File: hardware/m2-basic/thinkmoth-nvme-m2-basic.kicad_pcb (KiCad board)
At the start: 4 copper layers, 31 x 68.4 mm, 24 parts, among them J1 ExpressCard, J2 MDT180M03001, J3 TF-009, U1 GL823K-HCY04

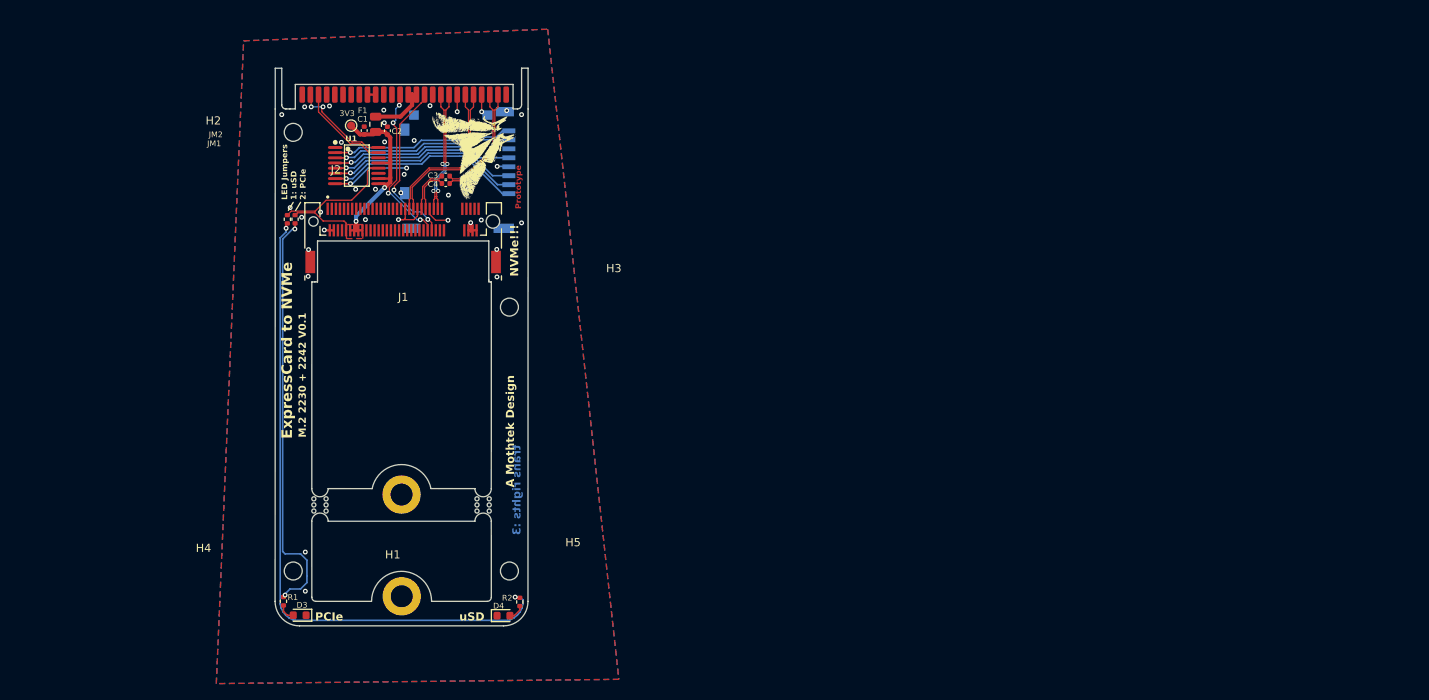
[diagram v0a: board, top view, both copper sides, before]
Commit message: README.md: added part list, changed some stuff
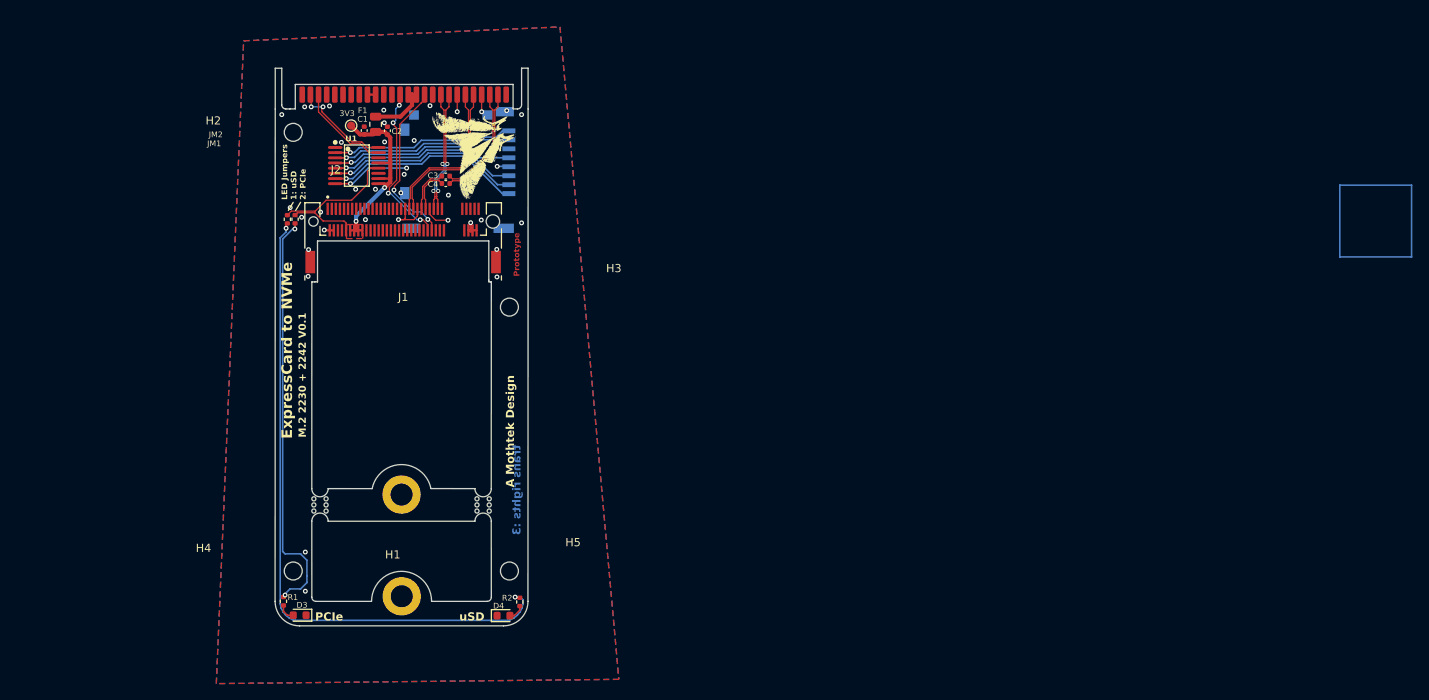
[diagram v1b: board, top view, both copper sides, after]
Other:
- board text removed: "NVMe!!!"
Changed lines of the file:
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@@
 		(layer "F.Mask")
 	)
+	(gr_rect
+		(start 190.7 63.6)
+		(end 199.5 72.4)
+		(stroke
+			(width 0.2)
+			(type solid)
+		)
+		(fill no)
+		(layer "B.Cu")
+	)
 	(gr_poly
 		(pts
@@
 	)
 	(gr_text "Prototype"
-		(at 90.4 66.525 90)
+		(at 90.2 74.8 90)
 		(layer "F.Cu")
 		(effects
@@
 		)
 	)
-	(gr_text "NVMe!!!\n"
-		(at 90.1 74.8 90)
-		(layer "F.SilkS")
-		(effects
-			(font
-				(size 1 1)
-				(thickness 0.25)
-				(bold yes)
-			)
-			(justify left bottom)
-		)
-	)
 	(gr_text "M.2 2230 + 2242 V0.1"
 		(at 64.05 94.55 90)
@@
 		(polygon
 			(pts
-				(xy 56.317702 45.906215) (xy 93.592702 44.481215) (xy 102.317702 124.181215) (xy 52.967702 124.706215)
+				(xy 56.317702 45.906215) (xy 95.1 44.2) (xy 102.317702 124.181215) (xy 52.967702 124.706215)
 			)
 		)
@@
 		(polygon
 			(pts
-				(xy 60.425 47.175) (xy 59.55 48.65) (xy 57.6 48.95) (xy 57.475 118.45) (xy 94.7 120.1) (xy 92.975 54.55)
+				(xy 60.425 47.175) (xy 59.55 48.65) (xy 57.6 48.95) (xy 57.475 118.45) (xy 94.7 120.1) (xy 93.4 54.7)
 				(xy 93.05 49.7) (xy 90.525 48.65)
 			)
@@
 		(polygon
 			(pts
-				(xy 56.3 46.6) (xy 94.9 46.7) (xy 94.1 68.3) (xy 57.6 68.3)
+				(xy 56.3 46.6) (xy 95.418469 46.701343) (xy 94.618519 68.3) (xy 57.6 68.3)
 			)
 		)

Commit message: Fixed PCIe caps that shouldn't exist, minor routing tweaks
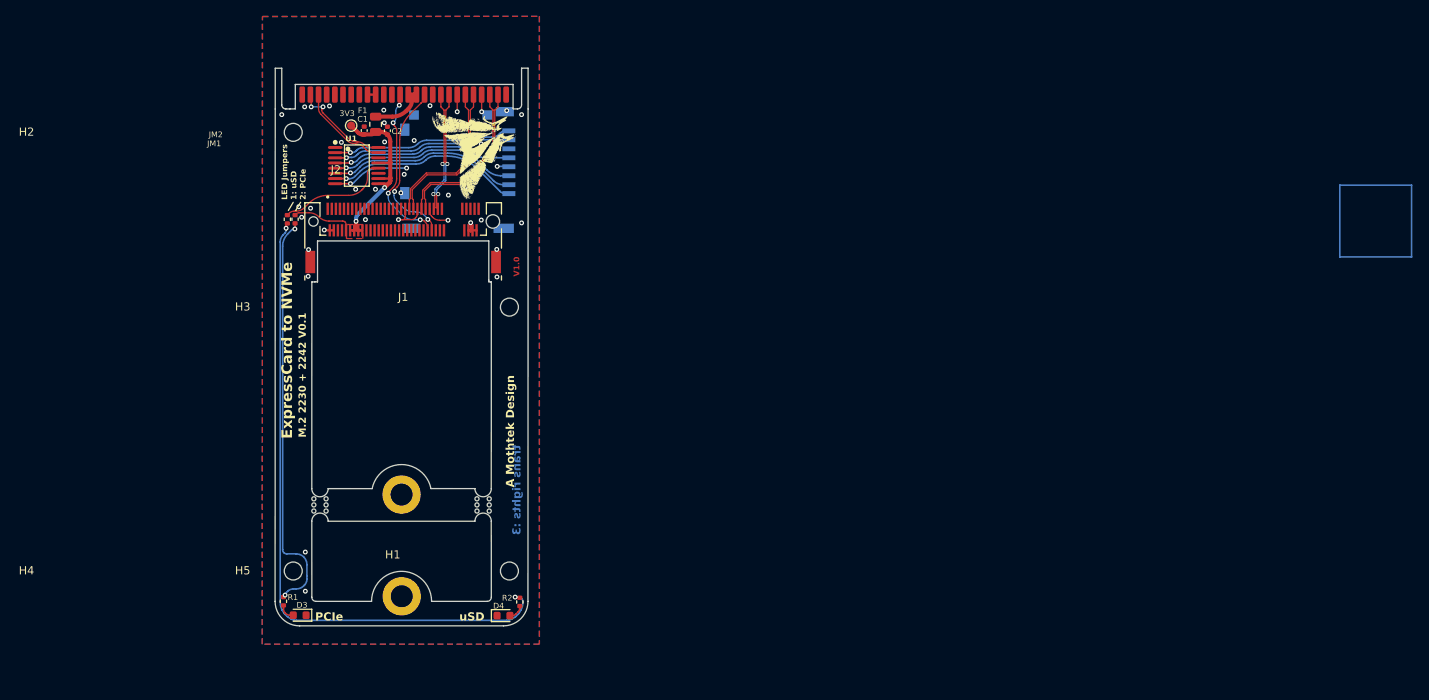
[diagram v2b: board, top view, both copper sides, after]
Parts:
- removed C3, C4: 0.1uF, Capacitor_SMD:C_0402_1005Metric
- H2, H3, H4, H5: value MOUNTING SCREW -> MH
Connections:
- J1 pad 24: PCIe_TX_C_N -> PCIe_TX_N
- J1 pad 25: PCIe_TX_C_P -> PCIe_TX_P
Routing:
- net PCIe_TX_P: track 5.30 -> 19.9 mm
- net PCIe_TX_N: track 5.67 -> 19.9 mm
- net PCIe_TX_C_P: track 14.2 -> 0.00 mm
- net PCIe_TX_C_N: track 13.8 -> 0.00 mm
- net 3V3: track 30.7 -> 31.7 mm
- net SD_DAT2: track 24.3 -> 23.7 mm
- net SD_DAT3: track 23.9 -> 23.3 mm
- net SD_CMD: track 23.5 -> 23.0 mm
- net LED_SD: track 14.5 -> 14.0 mm
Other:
- board text added: "V1.0"
- board text removed: "Prototype"
